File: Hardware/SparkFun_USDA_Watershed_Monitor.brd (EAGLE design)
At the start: 63.5 x 63.5 mm, 250 parts, among them J10 QWIIC_RIGHT_ANGLE, J12 3-PIN SMD, J3 QWIIC_RIGHT_ANGLE, J4 U.FL, J5 RJ45, J7 RJ45, J9 RJ45, Q1 20V/4.2A/52mΩ/1.4W, Q10 20V/4.2A/52mΩ/1.4W, Q11 20V/0.2A/8MHz/1.2Ω/1Vth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

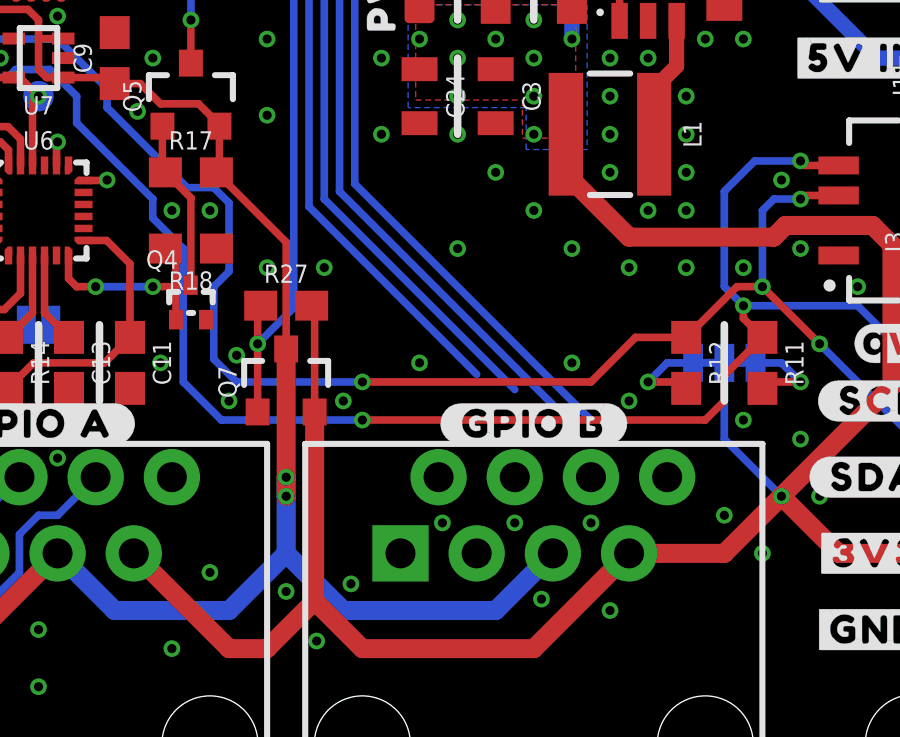
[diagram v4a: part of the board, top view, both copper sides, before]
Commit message: Update GPIO net names
Include both the ESP GPIO number, and the destination
Required schematic to be nudged around in a couple places
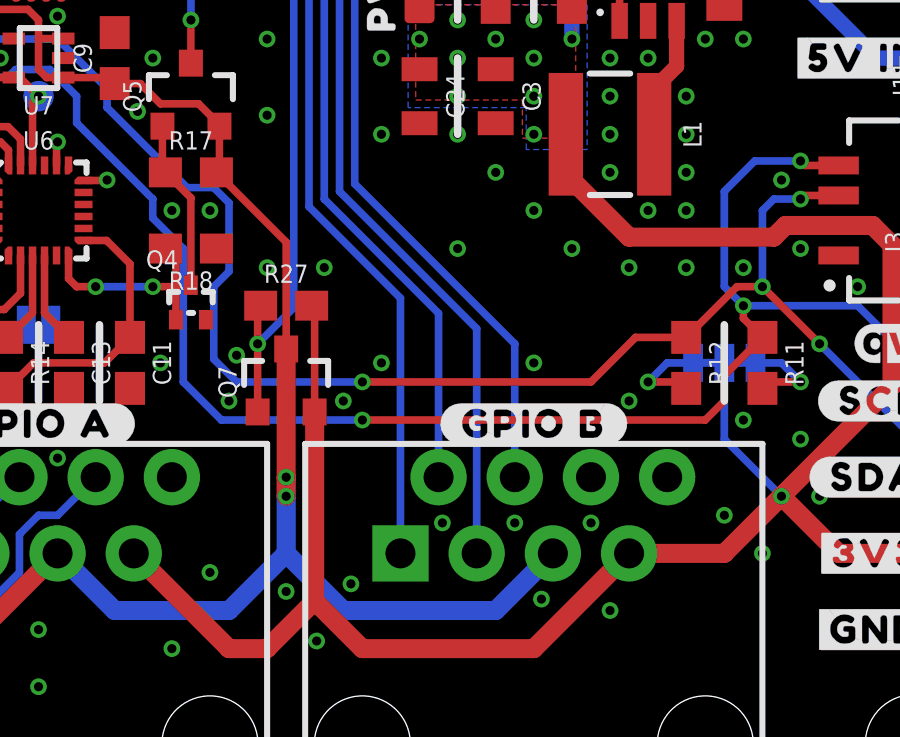
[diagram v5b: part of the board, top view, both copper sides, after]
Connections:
- net !RFM_CS! renamed ESP_IO15/!RFM_CS!
- net !RFM_RST! renamed ESP_IO5/!RFM_RST!
- net ESP_I36 renamed ESP_I36/GPS_TX
- net ESP_INT_COM renamed ESP_IO4/INT_COM
- net ESP_IO0_BOOT renamed ESP_IO0/BOOT
- net ESP_IO16 renamed ESP_IO16/VOUT
- net ESP_RX renamed ESP_IO3/ESP_RX
- net ESP_TX renamed ESP_IO1/ESP_TX
- net PICO renamed ESP_IO13/PICO
- net POCI renamed ESP_IO12/POCI
- net RFM_IO0 renamed ESP_IO27/RFM_IO0
- net RFM_IO1 renamed ESP_IO26/RFM_IO1
- net SCK renamed ESP_IO14/SCK
- net SCL renamed ESP_IO22/SCL
- net SDA renamed ESP_IO21/SDA
- net STAT renamed ESP_IO2/STAT
- net V_BATT_2 renamed ESP_IO32/V_BATT_2
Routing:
- net ESP_IO17: track 37.3 -> 42.2 mm
- net ESP_IO19: track 43.7 -> 47.6 mm
- net ESP_IO18: track 40.9 -> 42.7 mm
- net ESP_IO23: track 50.1 -> 51.0 mm
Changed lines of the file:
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@@
 <via x="39.37" y="26.035" extent="1-16" drill="0.3048"/>
 <via x="45.72" y="19.05" extent="1-16" drill="0.3048"/>
-<via x="49.53" y="15.24" extent="1-16" drill="0.3048"/>
+<via x="48.26" y="15.24" extent="1-16" drill="0.3048"/>
 <via x="39.37" y="23.495" extent="1-16" drill="0.3048"/>
 <via x="41.275" y="18.415" extent="1-16" drill="0.3048"/>
@@
 <via x="37.465" y="20.32" extent="1-16" drill="0.3048"/>
 <via x="38.1" y="13.97" extent="1-16" drill="0.3048"/>
-<via x="44.45" y="15.24" extent="1-16" drill="0.3048"/>
+<via x="43.18" y="15.24" extent="1-16" drill="0.3048"/>
 <via x="0.635" y="34.925" extent="1-16" drill="0.3048"/>
 <via x="0.635" y="28.575" extent="1-16" drill="0.3048"/>
@@
 <wire x1="20.32" y1="52.49" x2="21.25" y2="53.42" width="0.254" layer="1"/>
 </signal>
-<signal name="SCL">
+<signal name="ESP_IO22/SCL">
 <contactref element="J3" pad="4"/>
 <contactref element="U1" pad="36"/>
@@
 <wire x1="23.241" y1="26.67" x2="23.241" y2="34.036" width="0.254" layer="16"/>
 </signal>
-<signal name="SDA">
+<signal name="ESP_IO21/SDA">
 <contactref element="J3" pad="3"/>
 <contactref element="U1" pad="33"/>
@@
 <wire x1="35.56" y1="17.78" x2="36.33" y2="17.78" width="0.254" layer="1"/>
 </signal>
-<signal name="ESP_RX">
+<signal name="ESP_IO3/ESP_RX">
 <contactref element="U8" pad="2"/>
 <contactref element="U1" pad="34"/>
@@
 <wire x1="39.814" y1="51.435" x2="39.624" y2="51.435" width="0.254" layer="1"/>
 </signal>
-<signal name="ESP_TX">
+<signal name="ESP_IO1/ESP_TX">
 <contactref element="U8" pad="3"/>
 <contactref element="U1" pad="35"/>
@@
 <wire x1="26.2636" y1="33.8836" x2="27.305" y2="33.8836" width="0.254" layer="16"/>
 </signal>
-<signal name="RFM_IO0">
+<signal name="ESP_IO27/RFM_IO0">
 <contactref element="U11" pad="DIO0"/>
 <wire x1="2.26" y1="45.26" x2="4.27" y2="45.26" width="0.254" layer="1"/>
@@
 <wire x1="22.733" y1="38.1" x2="15.24" y2="38.1" width="0.254" layer="16"/>
 </signal>
-<signal name="POCI">
+<signal name="ESP_IO12/POCI">
 <contactref element="U11" pad="SDO"/>
 <contactref element="U1" pad="14"/>
@@
 <wire x1="20.219" y1="40.36" x2="21.129" y2="39.45" width="0.254" layer="1"/>
 </signal>
-<signal name="PICO">
+<signal name="ESP_IO13/PICO">
 <contactref element="U11" pad="SDI"/>
 <contactref element="U1" pad="16"/>
@@
 <wire x1="22.86" y1="36.322" x2="19.304" y2="39.878" width="0.254" layer="1"/>
 </signal>
-<signal name="SCK">
+<signal name="ESP_IO14/SCK">
 <contactref element="U11" pad="SCK"/>
 <contactref element="U1" pad="13"/>
@@
 <wire x1="45.339" y1="50.419" x2="45.339" y2="52.109" width="0.254" layer="1"/>
 </signal>
-<signal name="ESP_IO0_BOOT">
+<signal name="ESP_IO0/BOOT">
 <contactref element="Q6" pad="6"/>
 <contactref element="U1" pad="25"/>
@@
 <wire x1="46.1264" y1="40.22594375" x2="46.1264" y2="39.78405625" width="0.254" layer="1"/>
 </signal>
-<signal name="STAT">
+<signal name="ESP_IO2/STAT">
 <contactref element="U1" pad="24"/>
 <contactref element="D4" pad="A"/>
@@
 <wire x1="38.493" y1="36.678" x2="38.493" y2="35.56" width="0.254" layer="1"/>
 </signal>
-<signal name="ESP_INT_COM">
+<signal name="ESP_IO4/INT_COM">
 <contactref element="U1" pad="26"/>
 <contactref element="ICM_INT" pad="3"/>
@@
 <wire x1="40.67" y1="40.64" x2="40.75" y2="40.72" width="0.254" layer="1"/>
 </signal>
-<signal name="ESP_IO16">
+<signal name="ESP_IO16/VOUT">
 <contactref element="U1" pad="27"/>
 <contactref element="ISM_INT1" pad="1"/>
@@
 <wire x1="43.307" y1="40.005" x2="40.767" y2="37.465" width="0.254" layer="16"/>
 <wire x1="40.767" y1="37.465" x2="40.767" y2="20.447" width="0.254" layer="16"/>
-<wire x1="40.767" y1="20.447" x2="46.355" y2="14.859" width="0.254" layer="16"/>
+<wire x1="43.815" y1="17.399" x2="40.767" y2="20.447" width="0.254" layer="16"/>
 <contactref element="J9" pad="1"/>
-<wire x1="43.815" y1="8.89" x2="46.355" y2="14.859" width="0" layer="19" extent="16-16"/>
+<wire x1="43.815" y1="8.89" x2="43.815" y2="17.399" width="0.254" layer="16"/>
 </signal>
 <signal name="ESP_IO18">
@@
 <wire x1="43.815" y1="39.751" x2="41.275" y2="37.211" width="0.254" layer="16"/>
 <wire x1="41.275" y1="37.211" x2="41.275" y2="20.701" width="0.254" layer="16"/>
-<wire x1="41.275" y1="20.701" x2="47.625" y2="14.351" width="0.254" layer="16"/>
+<wire x1="41.275" y1="20.701" x2="45.085" y2="16.891" width="0.254" layer="16"/>
 <contactref element="J9" pad="2"/>
-<wire x1="45.085" y1="11.43" x2="47.625" y2="14.351" width="0" layer="19" extent="16-16"/>
+<wire x1="45.085" y1="16.891" x2="45.085" y2="11.43" width="0.254" layer="16"/>
 </signal>
 <signal name="ESP_IO19">
@@
 <wire x1="44.323" y1="39.497" x2="41.783" y2="36.957" width="0.254" layer="16"/>
 <wire x1="41.783" y1="36.957" x2="41.783" y2="20.955" width="0.254" layer="16"/>
-<wire x1="41.783" y1="20.955" x2="48.895" y2="13.843" width="0.254" layer="16"/>
+<wire x1="41.783" y1="20.955" x2="46.355" y2="16.383" width="0.254" layer="16"/>
 <contactref element="J9" pad="3"/>
-<wire x1="46.355" y1="8.89" x2="48.895" y2="13.843" width="0" layer="19" extent="16-16"/>
+<wire x1="46.355" y1="16.383" x2="46.355" y2="8.89" width="0.254" layer="16"/>
 </signal>
 <signal name="ESP_IO23">
@@
 <wire x1="44.831" y1="39.243" x2="42.291" y2="36.703" width="0.254" layer="16"/>
 <wire x1="42.291" y1="36.703" x2="42.291" y2="21.209" width="0.254" layer="16"/>
-<wire x1="42.291" y1="21.209" x2="50.165" y2="13.335" width="0.254" layer="16"/>
+<wire x1="47.625" y1="15.875" x2="42.291" y2="21.209" width="0.254" layer="16"/>
 <contactref element="J9" pad="4"/>
-<wire x1="47.625" y1="11.43" x2="50.165" y2="13.335" width="0" layer="19" extent="16-16"/>
+<wire x1="47.625" y1="11.43" x2="47.625" y2="15.875" width="0.254" layer="16"/>
 </signal>
 <signal name="ESP_IO25">
@@
 <wire x1="26.67" y1="11.43" x2="28.575" y2="11.43" width="0.254" layer="16"/>
 </signal>
-<signal name="RFM_IO1">
+<signal name="ESP_IO26/RFM_IO1">
 <contactref element="U1" pad="11"/>
 <wire x1="22.75" y1="43.26" x2="24.05" y2="43.26" width="0.254" layer="1"/>
@@
 <wire x1="23.114" y1="36.83" x2="15.24" y2="36.83" width="0.254" layer="16"/>
 </signal>
-<signal name="V_BATT_2">
+<signal name="ESP_IO32/V_BATT_2">
 <contactref element="U1" pad="8"/>
 <contactref element="R25" pad="1"/>
@@
 <wire x1="20.574" y1="16.002" x2="26.543" y2="10.033" width="0.254" layer="16"/>
 </signal>
-<signal name="ESP_I36">
+<signal name="ESP_I36/GPS_TX">
 <contactref element="U1" pad="4"/>
 <wire x1="22.75" y1="52.15" x2="22.67" y2="52.07" width="0.254" layer="1"/>
@@
 <wire x1="52.578" y1="51.435" x2="53.6" y2="51.435" width="0.254" layer="1"/>
 </signal>
-<signal name="!RFM_CS!">
+<signal name="ESP_IO15/!RFM_CS!">
 <contactref element="U1" pad="23"/>
 <wire x1="36.195" y1="37.96" x2="36.195" y2="38.354" width="0.254" layer="1"/>
@@
 <wire x1="15.875" y1="48.26" x2="16.875" y2="49.26" width="0.254" layer="1"/>
 </signal>
-<signal name="!RFM_RST!">
+<signal name="ESP_IO5/!RFM_RST!">
 <contactref element="U1" pad="29"/>
 <wire x1="40.75" y1="44.53" x2="40.433" y2="44.53" width="0.254" layer="1"/>

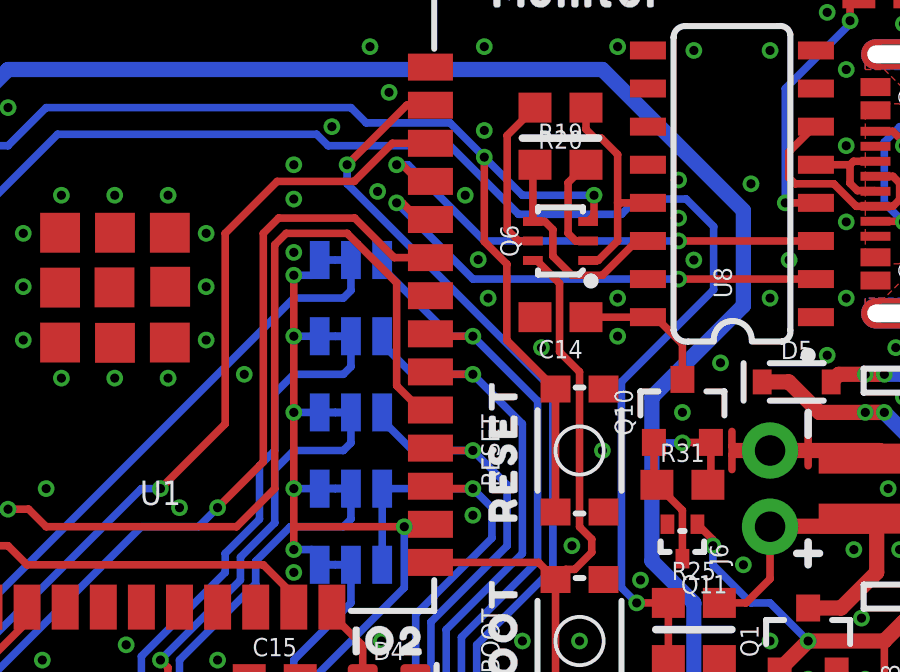
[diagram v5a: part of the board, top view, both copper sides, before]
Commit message: Reorder alternative interrupt pins
ESP16 was shared between an alternative interrupt, and the power control
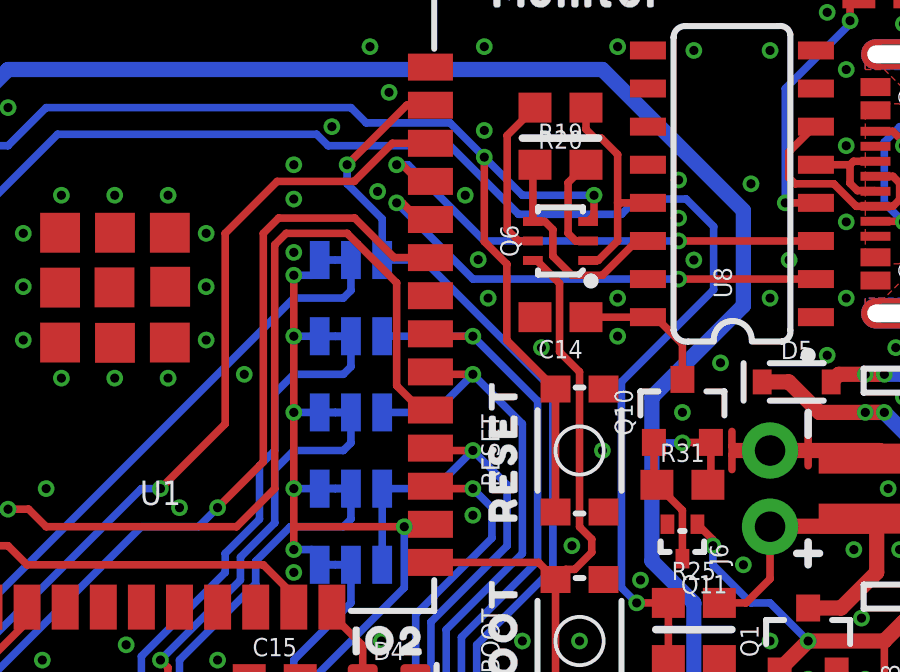
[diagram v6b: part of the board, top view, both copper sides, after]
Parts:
- removed U$69: (no value), output:#IO16#0
- added U$5: (no value), output:#IO17#0
- U$68: device output:#IO16#0 -> output:#IO23#0
- moved U$68 7.62 mm to (39.5, 49.5)
- moved U$67 2.54 mm to (39.5, 41.9)
- moved U$65 2.54 mm to (39.5, 47.0)
- moved U$66 2.54 mm to (39.5, 44.5)
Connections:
- net ESP_IO16/VOUT: no longer ICM_INT.1, ISM_INT1.1
- net ESP_IO17: now also ICM_INT.1, ISM_INT1.1; no longer ISM_INT2.1
- net ESP_IO18: now also ISM_INT2.1; no longer MMC_INT.1
- net ESP_IO19: now also MMC_INT.1; no longer NAU_INT.1
- net ESP_IO23: now also NAU_INT.1
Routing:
- net ESP_IO16/VOUT: track 38.4 -> 32.9 mm
- net ESP_IO17: track 42.2 -> 44.6 mm
- net ESP_IO19: track 47.6 -> 46.4 mm
- net ESP_IO23: track 51.0 -> 51.8 mm
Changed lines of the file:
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@@
 <element name="U$62" library="output" package="I350" value="" x="33.655" y="5.715" smashed="yes" rot="MR0"/>
 <element name="U$64" library="output" package="I390" value="" x="29.845" y="4.191" smashed="yes" rot="MR0"/>
-<element name="U$65" library="output" package="#IO19#0" value="" x="39.497" y="49.53" smashed="yes" rot="MR0"/>
-<element name="U$66" library="output" package="#IO18#0" value="" x="39.497" y="46.99" smashed="yes" rot="MR0"/>
-<element name="U$67" library="output" package="#IO17#0" value="" x="39.497" y="44.45" smashed="yes" rot="MR0"/>
-<element name="U$68" library="output" package="#IO16#0" value="" x="39.497" y="41.91" smashed="yes" rot="MR0"/>
-<element name="U$69" library="output" package="#IO16#0" value="" x="39.497" y="39.37" smashed="yes" rot="MR0"/>
+<element name="U$65" library="output" package="#IO19#0" value="" x="39.497" y="46.99" smashed="yes" rot="MR0"/>
+<element name="U$66" library="output" package="#IO18#0" value="" x="39.497" y="44.45" smashed="yes" rot="MR0"/>
+<element name="U$67" library="output" package="#IO17#0" value="" x="39.497" y="41.91" smashed="yes" rot="MR0"/>
 <element name="U$70" library="output" package="#NAU_INT#0" value="" x="36.703" y="49.53" smashed="yes" rot="MR0"/>
 <element name="U$71" library="output" package="#MMC_INT#0" value="" x="36.703" y="46.99" smashed="yes" rot="MR0"/>
@@
 <attribute name="VALUE" x="49.149" y="41.275" size="0.6096" layer="27" font="vector" ratio="20" align="top-center"/>
 </element>
+<element name="U$5" library="output" package="#IO17#0" value="" x="39.497" y="39.37" smashed="yes" rot="MR0"/>
+<element name="U$68" library="output" package="#IO23#0" value="" x="39.497" y="49.53" smashed="yes" rot="MR0"/>
 </elements>
 <signals>
@@
 <signal name="ESP_IO16/VOUT">
 <contactref element="U1" pad="27"/>
-<contactref element="ISM_INT1" pad="1"/>
-<contactref element="ICM_INT" pad="1"/>
-<wire x1="39.1414" y1="41.91" x2="42.164" y2="41.91" width="0.254" layer="16"/>
 <via x="42.164" y="41.91" extent="1-16" drill="0.3048"/>
 <wire x1="42.164" y1="41.91" x2="40.83" y2="41.91" width="0.254" layer="1"/>
 <wire x1="40.83" y1="41.91" x2="40.75" y2="41.99" width="0.254" layer="1"/>
-<wire x1="39.1414" y1="39.37" x2="39.1414" y2="41.91" width="0.254" layer="16"/>
 <wire x1="42.164" y1="41.91" x2="42.799" y2="41.275" width="0.254" layer="16"/>
 <wire x1="42.799" y1="41.275" x2="42.799" y2="40.259" width="0.254" layer="16"/>
@@
 <signal name="ESP_IO17">
 <contactref element="U1" pad="28"/>
-<contactref element="ISM_INT2" pad="1"/>
-<wire x1="40.1574" y1="43.18" x2="39.1414" y2="44.196" width="0.254" layer="16"/>
-<wire x1="39.1414" y1="44.45" x2="39.1414" y2="44.196" width="0.254" layer="16"/>
-<wire x1="40.1574" y1="43.18" x2="42.164" y2="43.18" width="0.254" layer="16"/>
 <via x="42.164" y="43.18" extent="1-16" drill="0.3048"/>
 <wire x1="42.164" y1="43.18" x2="40.83" y2="43.18" width="0.254" layer="1"/>
@@
 <contactref element="J9" pad="1"/>
 <wire x1="43.815" y1="8.89" x2="43.815" y2="17.399" width="0.254" layer="16"/>
+<contactref element="ISM_INT1" pad="1"/>
+<contactref element="ICM_INT" pad="1"/>
+<wire x1="39.1414" y1="39.37" x2="39.1414" y2="41.91" width="0.254" layer="16"/>
+<wire x1="39.1414" y1="41.91" x2="40.894" y2="41.91" width="0.254" layer="16"/>
+<wire x1="40.894" y1="41.91" x2="42.164" y2="43.18" width="0.254" layer="16"/>
 </signal>
 <signal name="ESP_IO18">
 <contactref element="U1" pad="30"/>
-<contactref element="MMC_INT" pad="1"/>
-<wire x1="39.1414" y1="46.99" x2="39.1414" y2="46.736" width="0.254" layer="16"/>
-<wire x1="40.1574" y1="45.72" x2="39.1414" y2="46.736" width="0.254" layer="16"/>
-<wire x1="40.1574" y1="45.72" x2="42.164" y2="45.72" width="0.254" layer="16"/>
 <via x="42.164" y="45.72" extent="1-16" drill="0.3048"/>
+<wire x1="40.894" y1="44.45" x2="42.164" y2="45.72" width="0.254" layer="16"/>
+<wire x1="40.894" y1="44.45" x2="39.1414" y2="44.45" width="0.254" layer="16"/>
 <wire x1="42.164" y1="45.72" x2="40.83" y2="45.72" width="0.254" layer="1"/>
 <wire x1="40.83" y1="45.72" x2="40.75" y2="45.8" width="0.254" layer="1"/>
@@
 <contactref element="J9" pad="2"/>
 <wire x1="45.085" y1="16.891" x2="45.085" y2="11.43" width="0.254" layer="16"/>
+<contactref element="ISM_INT2" pad="1"/>
 </signal>
 <signal name="ESP_IO19">
 <contactref element="U1" pad="31"/>
-<contactref element="NAU_INT" pad="1"/>
-<wire x1="41.4274" y1="46.99" x2="39.1414" y2="49.276" width="0.254" layer="16"/>
-<wire x1="39.1414" y1="49.53" x2="39.1414" y2="49.276" width="0.254" layer="16"/>
-<wire x1="41.4274" y1="46.99" x2="42.164" y2="46.99" width="0.254" layer="16"/>
+<wire x1="41.4274" y1="46.99" x2="41.91" y2="46.99" width="0.254" layer="16"/>
 <via x="42.164" y="46.99" extent="1-16" drill="0.3048"/>
+<wire x1="41.91" y1="46.99" x2="42.164" y2="46.99" width="0.254" layer="16"/>
 <wire x1="42.164" y1="46.99" x2="40.83" y2="46.99" width="0.254" layer="1"/>
 <wire x1="40.75" y1="47.07" x2="40.83" y2="46.99" width="0.254" layer="1"/>
@@
 <contactref element="J9" pad="3"/>
 <wire x1="46.355" y1="16.383" x2="46.355" y2="8.89" width="0.254" layer="16"/>
+<contactref element="MMC_INT" pad="1"/>
+<wire x1="41.4274" y1="46.99" x2="39.1414" y2="46.99" width="0.254" layer="16"/>
 </signal>
 <signal name="ESP_IO23">
@@
 <via x="37.973" y="52.705" extent="1-16" drill="0.3048"/>
 <wire x1="37.973" y1="52.705" x2="37.973" y2="52.07" width="0.254" layer="16"/>
-<wire x1="37.973" y1="52.07" x2="44.831" y2="45.212" width="0.254" layer="16"/>
+<wire x1="40.513" y1="49.53" x2="44.831" y2="45.212" width="0.254" layer="16"/>
 <wire x1="44.831" y1="45.212" x2="44.831" y2="39.243" width="0.254" layer="16"/>
 <wire x1="44.831" y1="39.243" x2="42.291" y2="36.703" width="0.254" layer="16"/>
@@
 <contactref element="J9" pad="4"/>
 <wire x1="47.625" y1="11.43" x2="47.625" y2="15.875" width="0.254" layer="16"/>
+<contactref element="NAU_INT" pad="1"/>
+<wire x1="39.1414" y1="49.53" x2="39.1414" y2="50.9016" width="0.254" layer="16"/>
+<wire x1="39.1414" y1="50.9016" x2="37.973" y2="52.07" width="0.254" layer="16"/>
+<wire x1="39.1414" y1="49.53" x2="40.513" y2="49.53" width="0.254" layer="16"/>
 </signal>
 <signal name="ESP_IO25">
